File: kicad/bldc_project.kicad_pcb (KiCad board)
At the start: 4 copper layers, 105 x 60 mm, 160 parts, among them J1 Conn_ARM_SWD_TagConnect_TC203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, J2 Screw_Terminal_01x03, J3 Screw_Terminal_01x03, J4 TYPE-C-31-M-12, Q1 IRFZ44N, Q2 IRFZ44N, Q3 IRFZ44N, Q4 IRFZ44N, Q5 IRFZ44N, Q6 IRFZ44N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

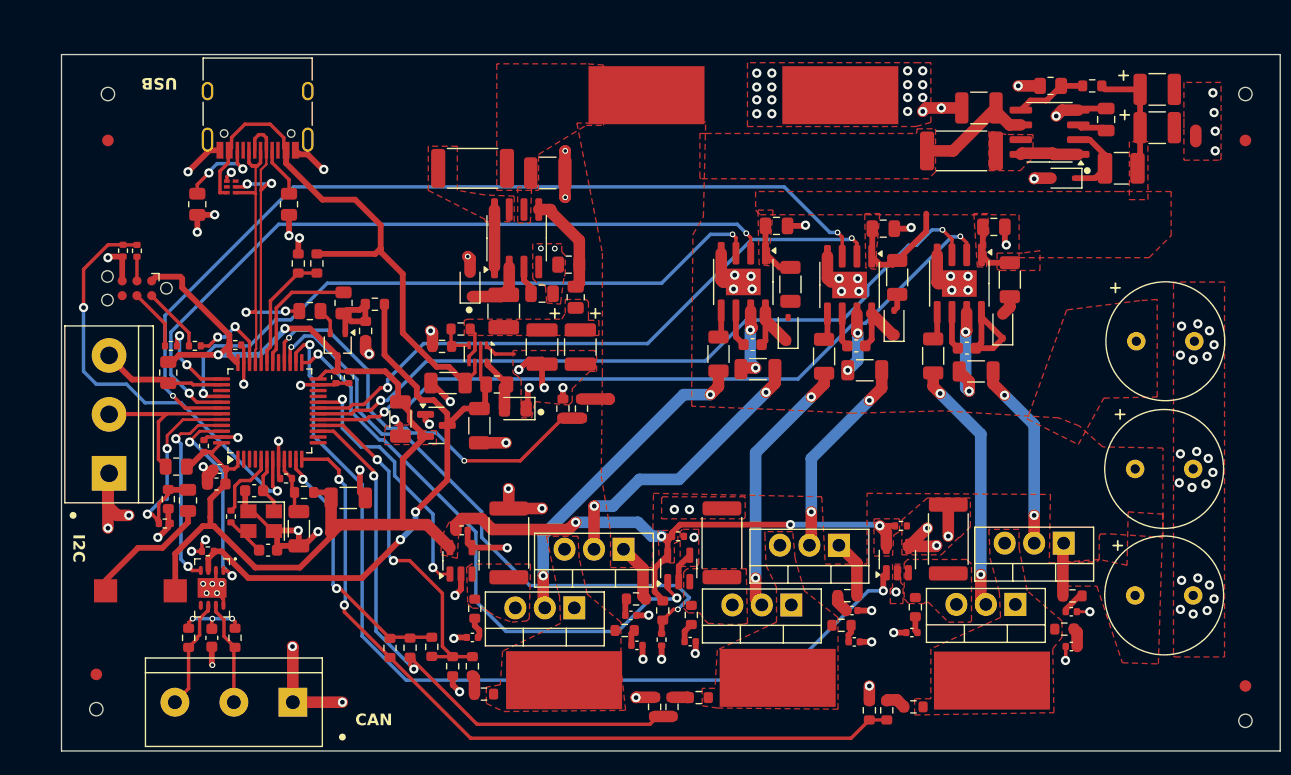
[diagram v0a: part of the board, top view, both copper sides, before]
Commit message: [kicad] Added return vias, added copper pours to balance out thermal / mechanical effects
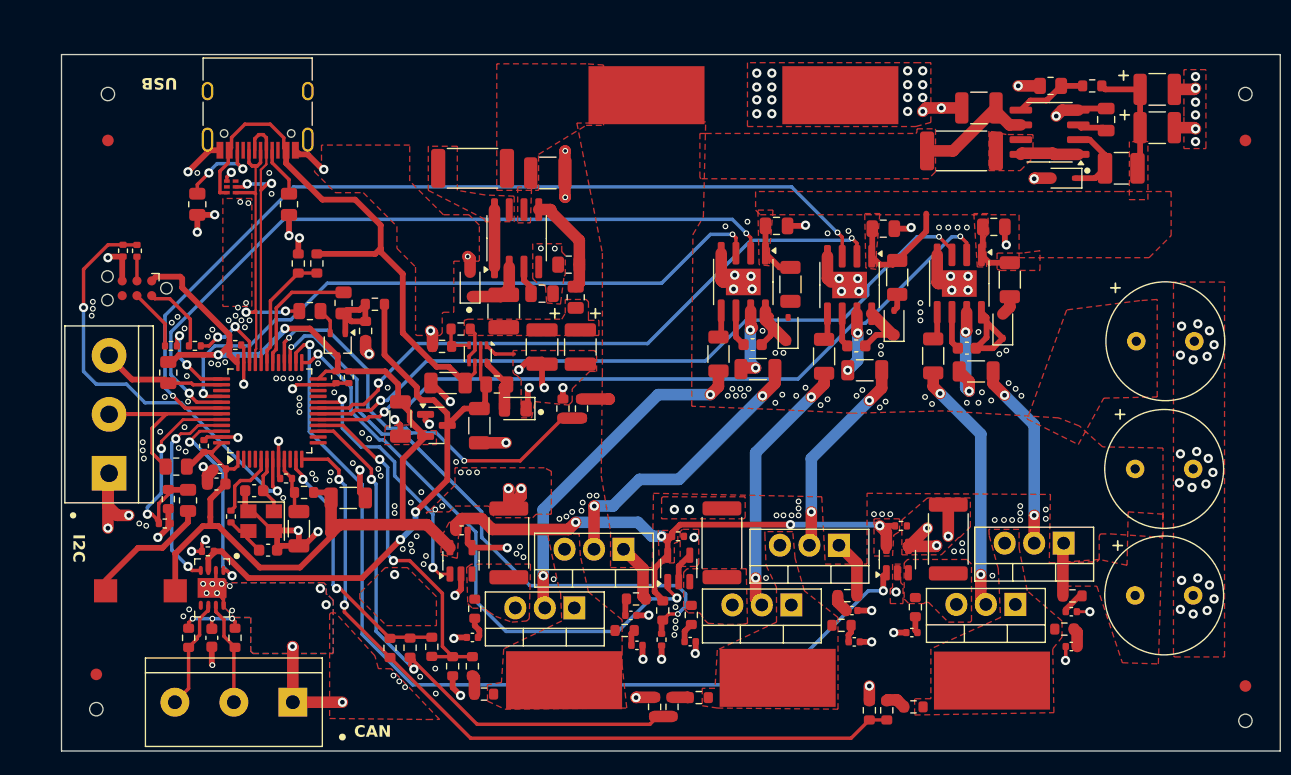
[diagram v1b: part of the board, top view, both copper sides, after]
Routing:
- net GND: track 170.4 -> 173.6 mm, vias 128 -> 296
- net Net-(Q6-G): track 28.1 -> 29.4 mm
- net PhaseU_SD: track 63.3 -> 62.3 mm
- net Net-(J1-SWDIO): track 5.66 -> 6.52 mm
- added copper zone on B.Cu, net GND

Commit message: [kicad] changed some footprints | TODO: Fix footprint of USB-ESD protection, recheck components, fix ERC errors
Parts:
- U9: footprint bldc:TI_USB-ESD_TPD4S012 -> bldc:TI_R-PUSON-N6
- moved FM4 9.43 mm to (138.2, 95.9)
- moved H1 9.43 mm to (138.2, 91.9)
- moved FM3 9.22 mm to (134.2, 136.9)
- moved H3 8.06 mm to (44.2, 91.9)
- moved H2 5.10 mm to (138.2, 136.9)
- moved C16 1.30 mm to (132.5, 105.3)
- moved C17 1.10 mm to (132.6, 116.3)
- moved FM1 1.00 mm to (44.2, 87.9)
- moved FM2 1.00 mm to (44.2, 132.9)
- moved C18 0.73 mm to (133.0, 127.3)
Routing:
- net Net-(D3-A): track 0.00 -> 1.47 mm
- net Net-(D3-K): track 6.71 -> 5.36 mm
- net /CPU/MEAS_TEMP: track 52.5 -> 53.0 mm
- net GND: track 173.6 -> 173.5 mm, vias 296 -> 304
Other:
- board size 105 x 60 mm -> 100 x 60 mm

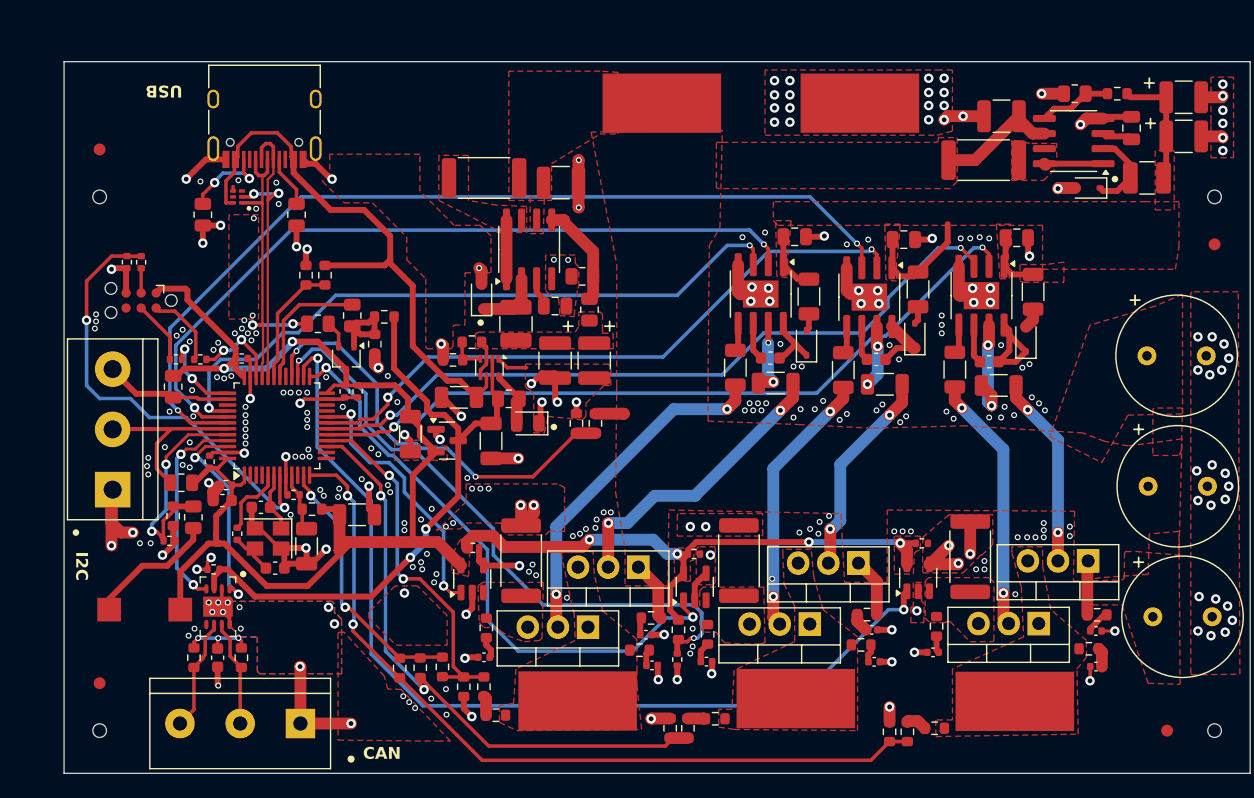
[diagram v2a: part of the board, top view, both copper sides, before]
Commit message: fixed erc errors
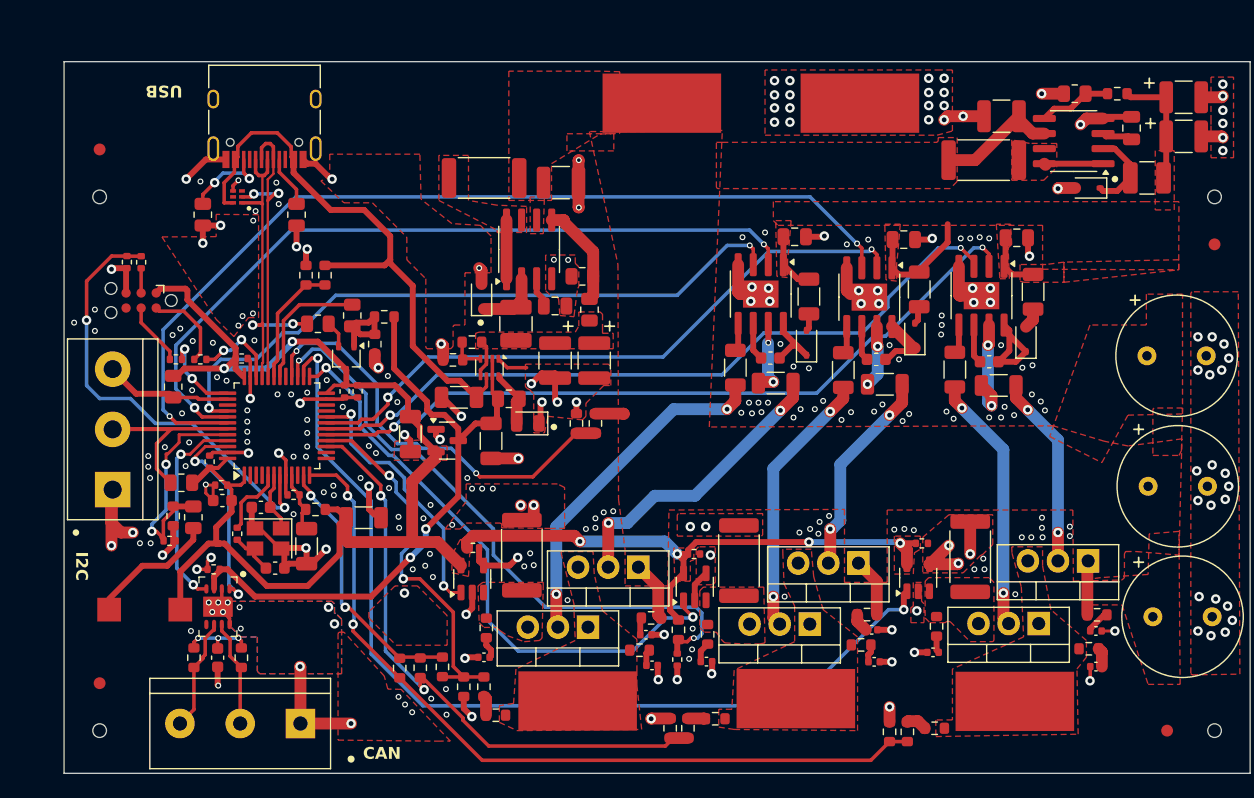
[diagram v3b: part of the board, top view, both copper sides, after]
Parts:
- moved C31 0.60 mm to (66.5, 119.0)
- moved R12 0.46 mm to (79.8, 122.1)
- moved C27 0.40 mm to (54.5, 116.2)
- moved FB1 0.30 mm to (62.4, 118.2)
- moved R2 0.10 mm to (113.3, 99.7)
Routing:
- net +3.3V: track 156.0 -> 154.1 mm
- net PhaseV_SD: track 78.2 -> 79.6 mm
- net Net-(D3-K): track 5.36 -> 6.53 mm
- net Net-(J1-SWDIO): track 6.52 -> 7.29 mm
- net PhaseW_DIV: track 30.4 -> 31.1 mm
- net /CPU/BOOT0: track 18.7 -> 19.2 mm
- net GND: track 173.5 -> 173.4 mm, vias 304 -> 283

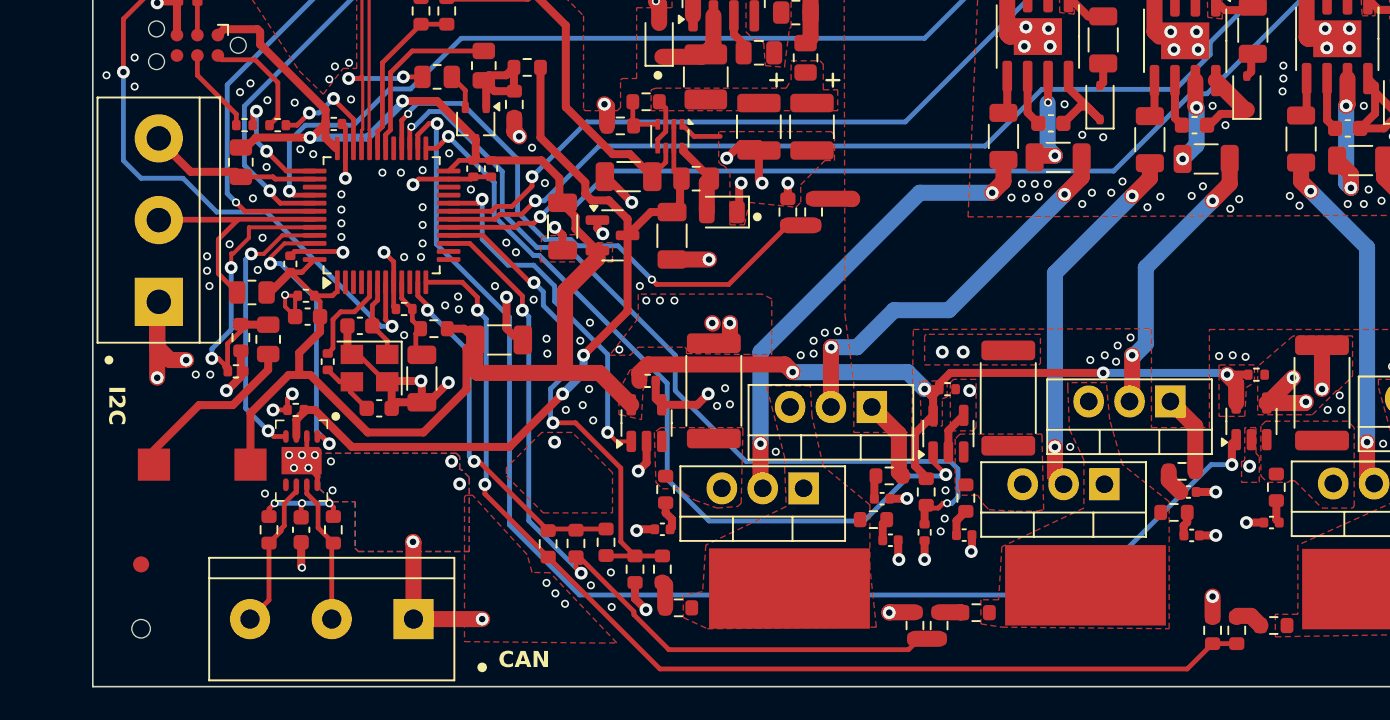
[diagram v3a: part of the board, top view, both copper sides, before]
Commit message: [kicad] Done first set of footprint checks, adapted connector to regular phoenix connector, found 3d models for everything but button [scripts] Checked resonator calculation [simulations] Checked bootstrap simulation [cubemx] Added extra GPIO-input + checked cpu pins
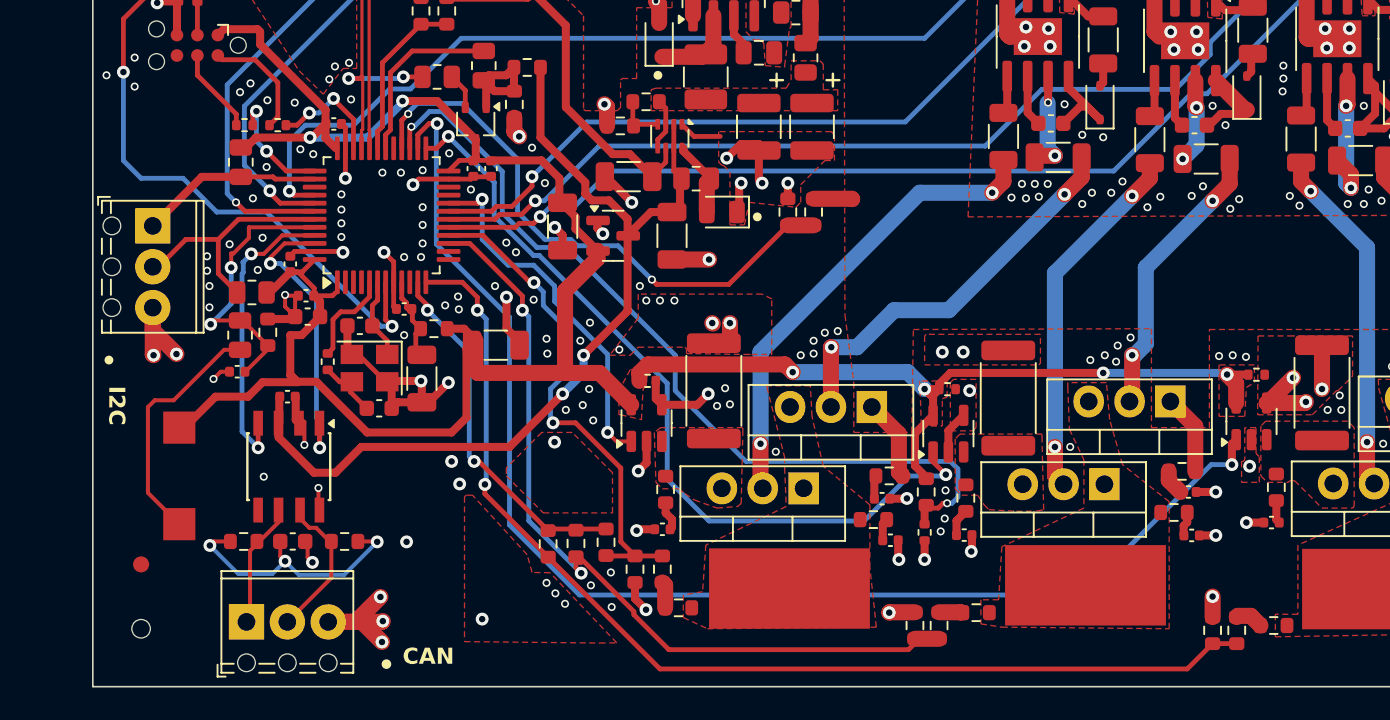
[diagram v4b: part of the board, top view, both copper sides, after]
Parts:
- C23, C24, C25, C26, C27, C28, C30, C33: footprint Resistor_SMD:R_0402_1005Metric -> Capacitor_SMD:C_0402_1005Metric
- J2: footprint bldc:Ningbo-Kangnex-Elec_3x1-WJ500V-5.08-3P -> TerminalBlock_Phoenix:TerminalBlock_Phoenix_MPT-0,5-3-2.54_1x03_P2.54mm_Horizontal
- J3: footprint TerminalBlock:TerminalBlock_bornier-3_P5.08mm -> TerminalBlock_Phoenix:TerminalBlock_Phoenix_MPT-0,5-3-2.54_1x03_P2.54mm_Horizontal
- U13: value ~ -> TPS2116DRLR
- U4, U5, U6: value INA180A2 -> INA180A2IDBVR
- U8: value ~ -> ATA6560-GAQW-N; footprint bldc:MICROCHIP_CAN_ATA6560-GAQW-N -> bldc:SOIC-8-N8_3.9x4.9mm_P1.27mm
- U9: value ~ -> TPD4S012DRYR
- moved J2 10.4 mm to (50.8, 136.5), turned to 0 degrees
- moved J3 4.73 mm to (44.9, 111.9), turned to -90 degrees
- moved R36 1.77 mm to (50.4, 118.7)
- moved R43 1.73 mm to (50.6, 131.5), turned to 180 degrees
- moved R37 1.71 mm to (52.1, 118.5), turned to 90 degrees
- moved SW1 1.59 mm to (46.6, 127.4), turned to -90 degrees
- moved R42 1.01 mm to (56.9, 131.5), turned to 180 degrees
- moved C33 0.97 mm to (53.3, 122.5), turned to 0 degrees
- moved C34 0.90 mm to (53.6, 131.5), turned to 0 degrees
- moved U8 0.88 mm to (53.4, 126.8), turned to -90 degrees
- moved C31 0.38 mm to (66.2, 119.3)
- moved C25 0.08 mm to (50.2, 120.9), turned to 180 degrees
- renumbered D7 to D4, D8 to D5, D9 to D6, U14 to U12
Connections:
- J2 pad 1: GND -> /CPU/CAN_L
- J2 pad 3: /CPU/CAN_L -> GND
- J3 pad 1: GND -> /CPU/I2C_SCL
- J3 pad 3: /CPU/I2C_SCL -> GND
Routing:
- net /CPU/CAN_N: track 6.19 -> 16.8 mm
- net /CPU/I2C_SDA: track 20.3 -> 15.1 mm
- net Net-(R36-Pad1): track 10.1 -> 15.3 mm
- net +3.3V: track 154.1 -> 158.0 mm
- net +5V: track 54.3 -> 57.6 mm
- net /CPU/CAN_L: track 10.0 -> 7.91 mm
- net /CPU/CAN_RX: track 17.4 -> 19.1 mm
- net /CPU/BOOT0: track 19.2 -> 17.7 mm
- net GND: track 173.4 -> 171.9 mm, vias 283 -> 278
- net /CPU/CAN_TX: track 17.5 -> 18.5 mm
- net /CPU/I2C_SCL: track 10.8 -> 11.4 mm
- removed copper zone on B.Cu, net GND
